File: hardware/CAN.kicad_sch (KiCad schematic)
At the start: 7 parts, among them U4 MCP2542FDxMF

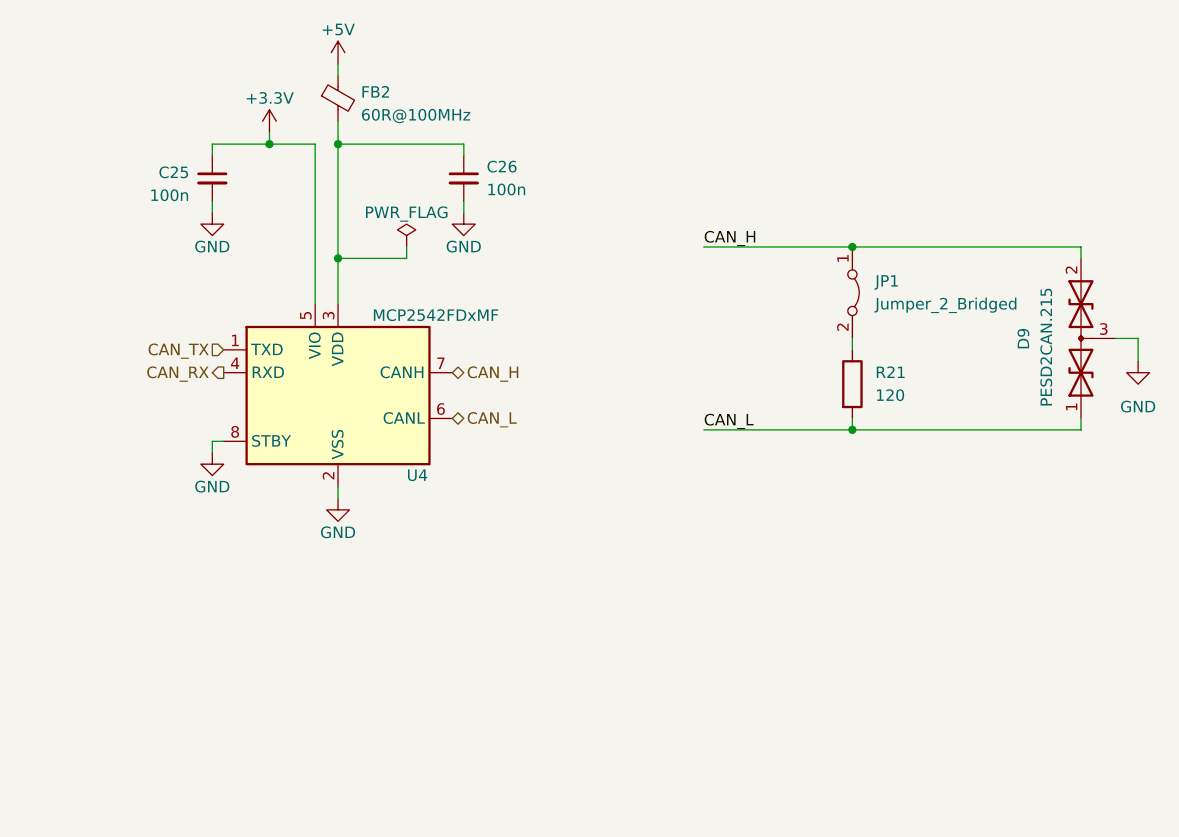
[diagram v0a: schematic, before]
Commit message: cube->cmake port, current calc fix, spi datalength fix, hard-v1.1.0 sync
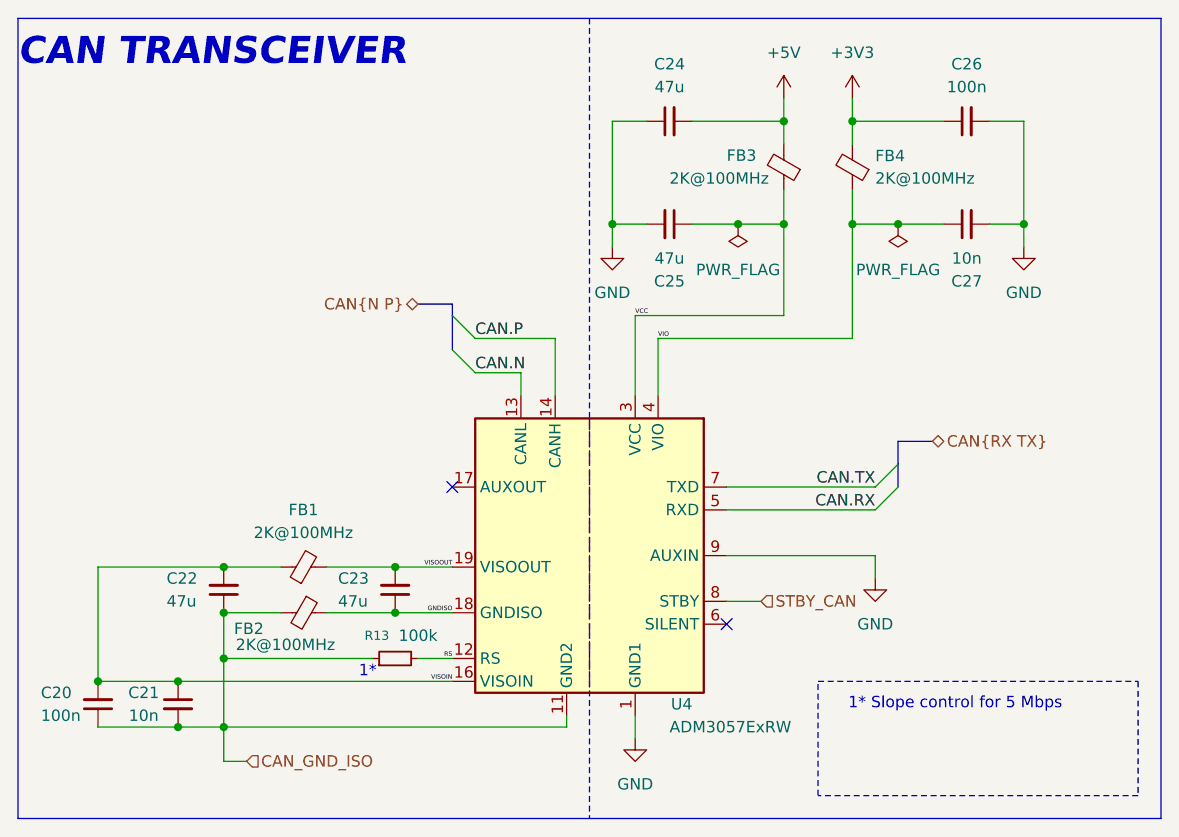
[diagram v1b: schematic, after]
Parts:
- removed D9: PESD2CAN.215, Package_TO_SOT_SMD:SOT-23, symbol BMS_LV_2022-rescue:D_TVS_x2_AAC-Device
- removed JP1: Jumper_2_Bridged, Connector_PinHeader_2.54mm:PinHeader_1x02_P2.54mm_Vertical, symbol Jumper:Jumper_2_Bridged
- removed R21: 120, Resistor_SMD:R_0603_1608Metric_Pad0.98x0.95mm_HandSolder, symbol Device:R
- removed U4: MCP2542FDxMF, Package_DFN_QFN:DFN-8-1EP_3x3mm_P0.65mm_EP1.55x2.4mm, symbol Interface_CAN_LIN:MCP2542FDxMF
- added C20: 100n, Capacitor_SMD:C_0603_1608Metric_Pad1.08x0.95mm_HandSolder, symbol Device:C_Small
- added C21, C27: 10n, Capacitor_SMD:C_0603_1608Metric_Pad1.08x0.95mm_HandSolder, symbol Device:C_Small
- added C22, C23, C24: 47u, Capacitor_SMD:C_0805_2012Metric_Pad1.18x1.45mm_HandSolder, symbol Device:C_Small
- added FB1, FB3, FB4: 2K@100MHz, Inductor_SMD:L_0805_2012Metric_Pad1.05x1.20mm_HandSolder, symbol Device:FerriteBead_Small
- added R13: 100k, Resistor_SMD:R_0603_1608Metric_Pad0.98x0.95mm_HandSolder, symbol Device:R_Small
- added U4: ADM3057ExRW, Package_SO:SOIC-20W_7.5x12.8mm_P1.27mm, symbol Interface_CAN_LIN:ADM3057ExRW
- C25: value 100n -> 47u; footprint Capacitor_SMD:C_0603_1608Metric_Pad1.08x0.95mm_HandSolder -> Capacitor_SMD:C_0805_2012Metric_Pad1.18x1.45mm_HandSolder; Done? (none) -> y; Mouser Part Number (none) -> 81-GRM21BR60J476M01K; Mouser Price/Stock (none) -> https://www.mouser.pl/ProductDetail/Murata-Electronics/GRM2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
- C26: Done? (none) -> y; Mouser Part Number (none) -> 81-GCJ188R71H104KA2D; Mouser Price/Stock (none) -> https://www.mouser.pl/ProductDetail/Murata-Electronics/GCJ1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
- FB2: value 60R@100MHz -> 2K@100MHz; footprint Inductor_SMD:L_0603_1608Metric -> Inductor_SMD:L_0805_2012Metric_Pad1.05x1.20mm_HandSolder; Done? (none) -> y; Mouser Part Number (none) -> 623-2508052027Y1; Mouser Price/Stock (none) -> https://www.mouser.pl/ProductDetail/Fair-Rite/2508052027Y1?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
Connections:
- net +5V: now also C24.2, FB3.2; no longer FB2.1
- net GND: now also C24.1, C27.2, U4.1 (GND1), U4.10 (GND1), U4.2 (GND1), U4.9 (AUXIN)
- net +3V3: now reaches C26.1
- net +3V3: now also FB4.2; no longer FB2.2
- net +3.3V renamed VCC
- net VCC: now also FB3.1, U4.3 (VCC)
- new net CAN.N: U4.13 (CANL)
- new net CAN.P: U4.14 (CANH)
- new net CAN.RX: U4.5 (RXD)
- new net CAN.TX: U4.7 (TXD)
- new net CAN_GND_ISO: C20.1, C21.2, C22.1, FB2.2, R13.1, U4.11 (GND2), U4.15 (GND2)
- new net GNDISO: C23.1, FB2.1, U4.18 (GNDISO), U4.20 (GNDISO)
- new net RS: R13.2, U4.12 (RS)
- new net STBY_CAN: U4.8 (STBY)
- new net VIO: C27.1, FB4.1, U4.4 (VIO)
- new net VISOIN: C20.2, C21.1, C22.2, FB1.1, U4.16 (VISOIN)
- new net VISOOUT: C23.2, FB1.2, U4.19 (VISOOUT)
- no-connect marks 0 -> 2
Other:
- note added: "1*"
- note added: "1* Slope control for 5 Mbps"
- note added: "CAN TRANSCEIVER"
- company: (none) -> Authors: Grzegorz Potocki Jędrzej Kasprzyk
- title: (none) -> PDUv3
